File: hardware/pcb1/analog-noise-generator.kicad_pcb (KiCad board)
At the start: 2 copper layers, 12.7 x 53 mm, 77 parts, among them J1 USB_C_Receptacle_USB2.0, J2 Conn_01x03_Pin, J5 Conn_01x04_Pin, J6 Conn_01x04_Pin, J7 Conn_01x02_Pin, J9 Conn_02x04_Odd_Even, U1 STM32F072CBTx, U2 USBLC6-2SC6, U3 LR8321A-T33, U4 LIS2DH12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

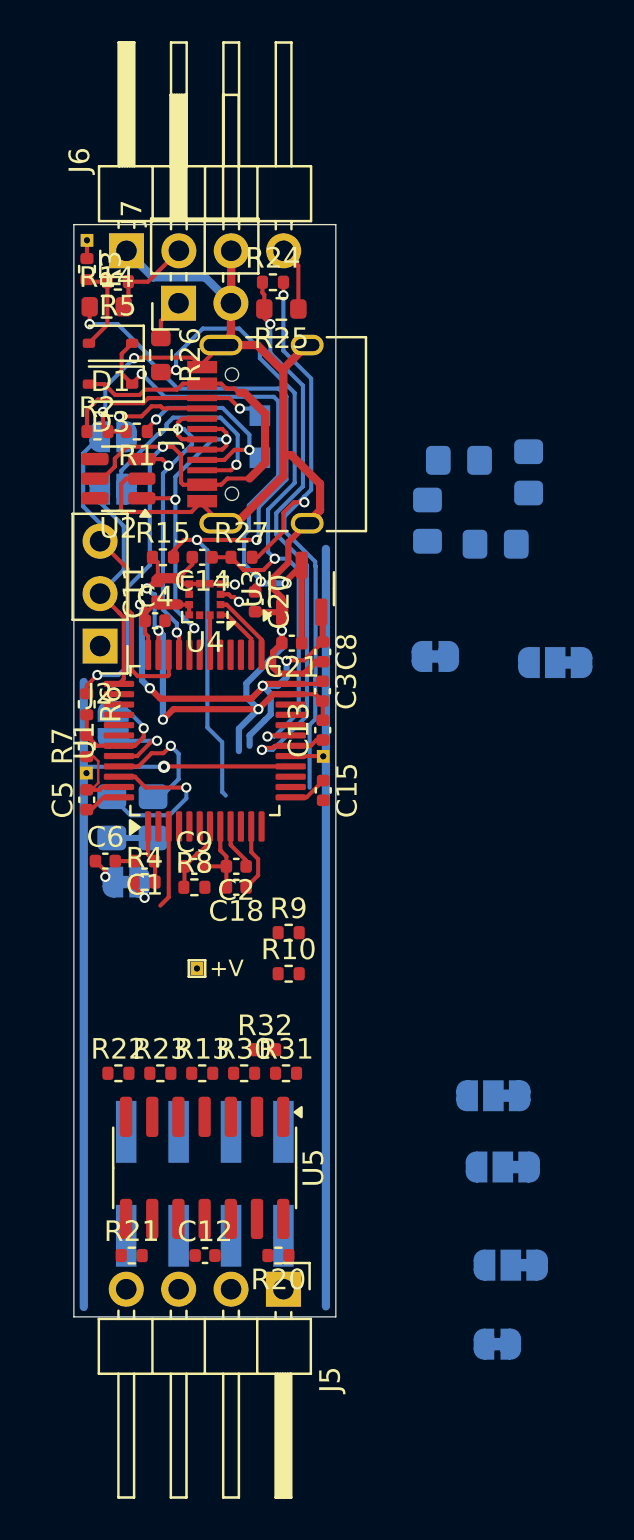
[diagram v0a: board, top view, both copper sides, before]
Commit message: switch to four layers and continue routing
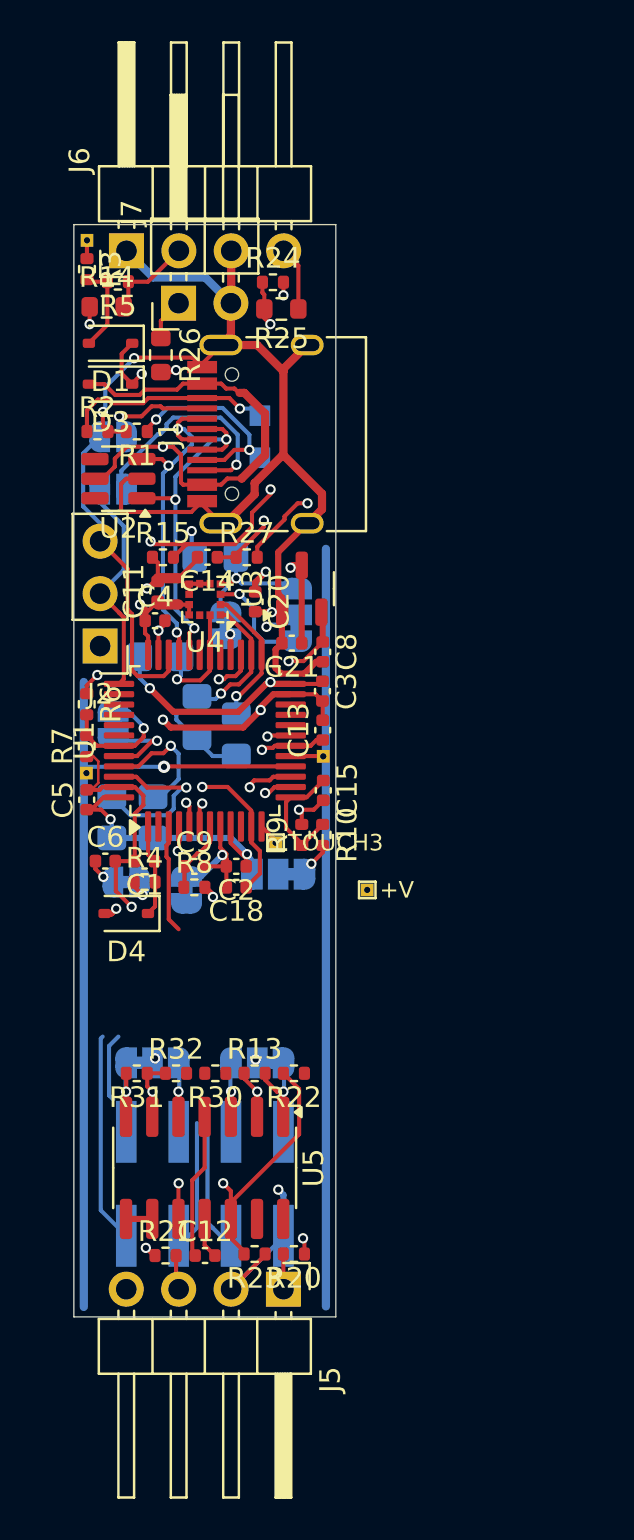
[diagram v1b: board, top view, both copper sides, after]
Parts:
- added D4: ~, Diode_SMD:D_SOD-323, F.Cu at (108.0, 89.9)
- added TP8: TOUCH3, analog-noise-generator:TestPoint_THTPad_small, F.Cu at (115.2, 86.5)
- moved JP12 26.7 mm to (110.9, 88.8), turned to -90 degrees
- moved JP10 22.1 mm to (115.3, 88.0)
- moved R16 19.1 mm to (113.3, 81.3), turned to -90 degrees
- moved JP6 17.7 mm to (109.2, 97.2), turned to 0 degrees
- moved R17 16.7 mm to (111.4, 80.4), turned to -90 degrees
- moved R19 14.5 mm to (109.6, 77.5), turned to 180 degrees
- moved JP8 12.8 mm to (116.2, 75.4), turned to 90 degrees
- moved R18 12.7 mm to (112.3, 72.6)
- moved JP4 11.6 mm to (114.3, 97.2)
- moved JP5 10.3 mm to (112.8, 75.9), turned to 90 degrees
- moved R23 9.88 mm to (114.2, 106.4), turned to 180 degrees
- moved TP4 9.09 mm to (119.6, 88.8)
- moved R22 8.51 mm to (116.1, 97.7), turned to 180 degrees
- moved R31 7.24 mm to (108.5, 97.7), turned to 180 degrees
- moved R10 6.93 mm to (117.5, 86.1), turned to -90 degrees
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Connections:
- net Net-(JP10-C) renamed /AVCC
- net Net-(JP12-B) renamed /AGND
- JP4 pad 2: /OUT1 -> Net-(JP4-C)
- JP6 pad 2: /OUT2 -> Net-(JP6-C)
- R13 pad 2: Net-(R13-Pad2) -> Net-(JP4-A)
- R20 pad 1: Net-(R13-Pad2) -> Net-(JP4-C)
- R20 pad 2: Net-(JP4-A) -> /OUT1
- R21 pad 1: Net-(R21-Pad1) -> Net-(JP6-C)
- R21 pad 2: Net-(JP6-A) -> /OUT2
- R31 pad 2: Net-(R21-Pad1) -> Net-(JP6-A)
- U1 pad 12: unconnected-(U1-PA2-Pad12) -> /TOUCH3
- U5 pad 1: Net-(R13-Pad2) -> Net-(JP4-A)
- U5 pad 7: Net-(R21-Pad1) -> Net-(JP6-A)
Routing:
- net GND: track 96.0 -> 148.4 mm, vias 7 -> 11
- net +3.3V: track 32.3 -> 69.2 mm, vias 4 -> 9
- net /SCK: track 2.74 -> 24.1 mm, vias 0 -> 1
- net +8V: track 26.9 -> 43.9 mm, vias 3 -> 4
- net Net-(U5C-+): track 0.00 -> 16.5 mm, vias 0 -> 2
- net /MOSI: track 0.00 -> 16.4 mm, vias 0 -> 1
- net /EPD_BUSY: track 4.01 -> 15.5 mm
- net Net-(JP4-C): track 0.00 -> 10.4 mm, vias 0 -> 2
- net Net-(JP6-C): track 0.00 -> 10.4 mm, vias 0 -> 2
- net /EPD_DC: track 0.00 -> 10.3 mm, vias 0 -> 1
- net /EPD_RES: track 0.00 -> 10.1 mm, vias 0 -> 1
- net /DAC2: track 0.00 -> 9.72 mm, vias 0 -> 2
- net /DAC1: track 0.00 -> 8.41 mm, vias 0 -> 2
- net /MISO: track 0.00 -> 7.21 mm, vias 0 -> 2
- net /AVCC: track 0.00 -> 7.03 mm
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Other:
- copper layers 2 -> 4

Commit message: finish routing
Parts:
- added TP10: AGND, analog-noise-generator:TestPoint_THTPad_small, B.Cu at (106.7, 96.5)
- added TP11: AVCC, analog-noise-generator:TestPoint_THTPad_small, B.Cu at (106.7, 95.5)
- added TP9: GND, analog-noise-generator:TestPoint_THTPad_small, B.Cu at (116.8, 96.5)
- TP4: moved to B.Cu
- moved JP6 7.42 mm to (110.1, 89.8)
- moved JP4 7.41 mm to (115.1, 89.8)
- moved R13 7.38 mm to (114.6, 90.3)
- moved R22 7.38 mm to (116.5, 90.3)
- moved C12 7.37 mm to (111.8, 99.1)
- moved J9 7.37 mm to (111.8, 95.7)
- moved R20 7.37 mm to (116.1, 99.1)
- moved R21 7.37 mm to (109.9, 99.1)
- moved R23 7.37 mm to (114.2, 99.1)
- moved R30 7.37 mm to (112.3, 90.3)
- moved R31 7.37 mm to (108.5, 90.3)
- moved R32 7.37 mm to (110.4, 90.3)
- moved U5 7.37 mm to (111.8, 94.9)
- moved J5 7.29 mm to (115.6, 100.8)
- moved TP4 7.29 mm to (116.8, 95.5), turned to 180 degrees
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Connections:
- U1 pad 4: /EPD_DC -> /EPD_CS
- U1 pad 5: /EPD_CS -> /EPD_RES
- U1 pad 6: /EPD_RES -> /EPD_DC
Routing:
- net /Vmiddle: track 37.7 -> 55.7 mm, vias 2 -> 3
- net /AGND: track 1.98 -> 19.4 mm, vias 0 -> 2
- net /AVCC: track 7.03 -> 22.7 mm, vias 0 -> 2
- net GND: track 148.4 -> 161.5 mm
- net +3.3V: track 69.2 -> 78.4 mm, vias 9 -> 11
- net /TOUCH1: track 40.4 -> 33.0 mm
- net /TOUCH2: track 38.5 -> 31.1 mm
- net +8V: track 43.9 -> 51.3 mm
- net /EPD_DC: track 10.3 -> 16.5 mm, vias 1 -> 2
- net /MOSI: track 16.4 -> 21.9 mm, vias 1 -> 2
- net /DAC2: track 9.72 -> 14.0 mm, vias 2 -> 3
- net /EPD_CS: track 6.73 -> 10.4 mm, vias 1 -> 2
- net /SCK: track 24.1 -> 27.8 mm, vias 1 -> 2
- net /DAC1: track 8.41 -> 11.6 mm, vias 2 -> 3
- net /EPD_RES: track 10.1 -> 11.5 mm, vias 1 -> 2
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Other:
- board size 12.7 x 53 mm -> 12.7 x 45.6 mm

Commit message: improve silk
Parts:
- added QR1: QR_git_3.8, analog-noise-generator-qr:QR_git_3.8, B.Cu at (107.6, 61.8)
- TP6: value TOUCH1 -> T1
- TP7: value TOUCH2 -> T2
- TP8: value TOUCH3 -> T3; moved to B.Cu
- moved TP8 0.25 mm to (115.2, 85.5), turned to 180 degrees
- turned D1 to 0 degrees
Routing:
- net /IN2L: track 32.4 -> 28.9 mm
- net +8V: track 51.3 -> 49.8 mm
- net GND: track 161.5 -> 160.7 mm, vias 11 -> 10
- net Net-(J1-CC1): track 9.95 -> 9.31 mm
- net /Vmiddle: track 55.7 -> 55.1 mm
- net /VIN_sense: track 47.0 -> 47.5 mm
- net +3.3V: track 78.4 -> 77.9 mm
- net Net-(U5A--): track 3.64 -> 3.48 mm, vias 1 -> 0
- net Net-(U5B--): track 3.20 -> 3.10 mm, vias 1 -> 0
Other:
- board text added: "1"
- board text added: "2"
- board text added: "3V3"
- board text added: "G"
- board text added: "GATE"
- board text added: "GND"
- board text added: "IN1"
- board text added: "IN2"
- board text added: "SWCLK"
- board text added: "SWDIO"
- board text added: "analog noise"
- board text added: "snowball"
- board text added: "v1"

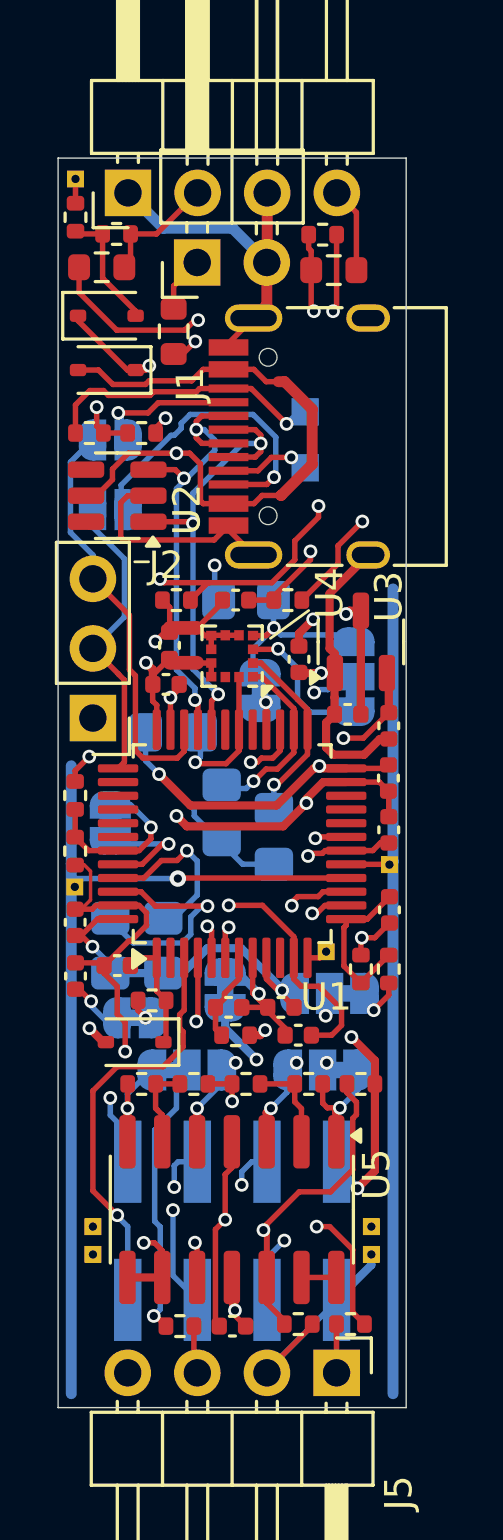
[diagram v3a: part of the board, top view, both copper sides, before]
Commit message: add some LEDs
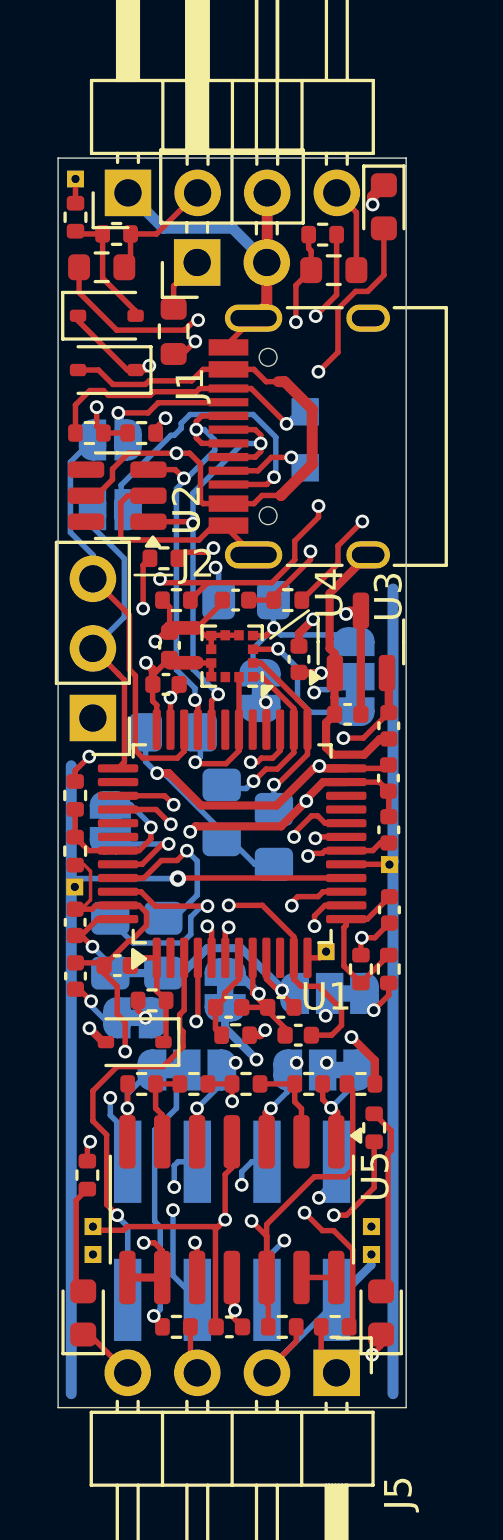
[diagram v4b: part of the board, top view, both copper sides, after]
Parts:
- added D5: white, LED_SMD:LED_0603_1608Metric, F.Cu at (117.2, 98.7)
- added D6: yellow, LED_SMD:LED_0603_1608Metric, F.Cu at (106.3, 98.7)
- added D7: red, LED_SMD:LED_0603_1608Metric, F.Cu at (117.3, 58.3)
- added R33: 1k, Resistor_SMD:R_0402_1005Metric, F.Cu at (116.9, 91.9)
- added R34: 2k2, Resistor_SMD:R_0402_1005Metric, F.Cu at (106.5, 93.6)
- added R35: 2k2, Resistor_SMD:R_0402_1005Metric, F.Cu at (109.3, 71.1)
- TP6: value T1 -> TOUCH1
- TP7: value T2 -> TOUCH2
- TP8: value T3 -> TOUCH3
- moved R23 0.59 mm to (113.6, 99.2)
- moved R20 0.57 mm to (115.5, 99.2)
- moved R21 0.13 mm to (109.7, 99.2)
- moved C12 0.11 mm to (111.7, 99.2)
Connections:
- U1 pad 20: unconnected-(U1-PB2-Pad20) -> /LED1
- U1 pad 39: unconnected-(U1-PB3-Pad39) -> /LED3
- U1 pad 40: unconnected-(U1-PB4-Pad40) -> /LED2
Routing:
- net /LED1: track 0.00 -> 23.2 mm, vias 0 -> 2
- net /LED2: track 0.00 -> 17.9 mm, vias 0 -> 2
- net Net-(D7-A): track 0.00 -> 16.9 mm, vias 0 -> 2
- net /LED3: track 0.00 -> 12.6 mm, vias 0 -> 2
- net GND: track 160.7 -> 172.4 mm, vias 10 -> 12
- net Net-(D5-A): track 0.00 -> 6.89 mm
- net Net-(D6-A): track 0.00 -> 4.01 mm
- net +3.3V: track 77.9 -> 80.8 mm
- net /Vmiddle: track 55.1 -> 56.3 mm
- net /DAC2: track 14.0 -> 13.3 mm

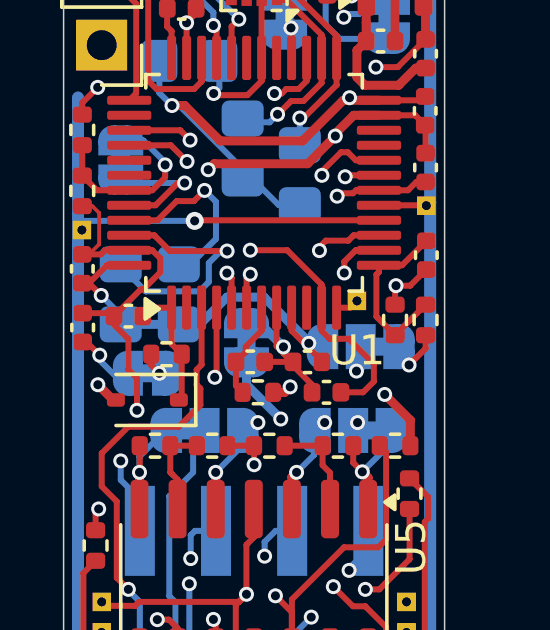
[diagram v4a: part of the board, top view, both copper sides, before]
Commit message: add testpoint for 3.3V
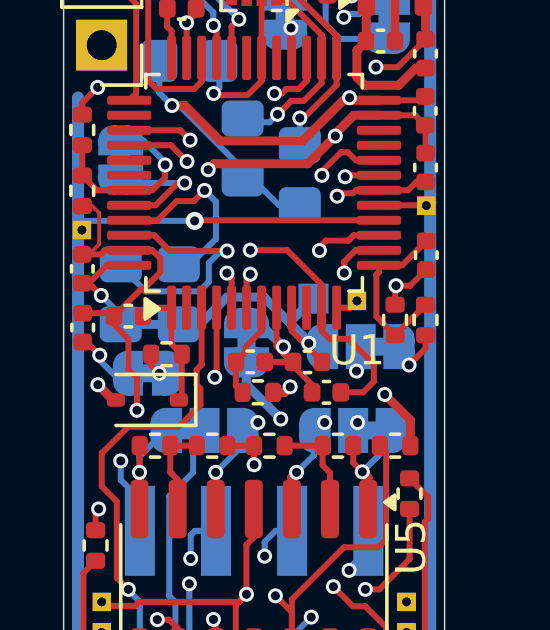
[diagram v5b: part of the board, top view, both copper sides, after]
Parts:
- added TP12: 3V3, TestPoint:TestPoint_Pad_1.0x1.0mm, B.Cu at (113.7, 85.4)
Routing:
- net +3.3V: track 80.8 -> 81.9 mm
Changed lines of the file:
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@@
     (property "ki_keywords" "R res resistor")
     (attr smd exclude_from_bom)
-    (fp_text reference "R16" (at 0.381 -1.397 90) (layer "B.SilkS")
+    (fp_text reference "R16" (at 0.3048 -1.27 90) (layer "B.SilkS")
         (effects (font (size 0.8 0.8) (thickness 0.12)) (justify mirror))
     )
@@
       ))
   )
+  (footprint "TestPoint:TestPoint_Pad_1.0x1.0mm" (layer "B.Cu")
+    (at 113.7412 85.3948)
+    (descr "SMD rectangular pad as test Point, square 1.0mm side length")
+    (tags "test point SMD pad rectangle square")
+    (property "Sheetfile" "analog-noise-generator.kicad_sch")
+    (property "Sheetname" "")
+    (property "exclude_from_bom" "")
+    (property "ki_description" "test point (alternative probe-style design)")
+    (property "ki_keywords" "test point tp")
+    (attr exclude_from_pos_files exclude_from_bom)
+    (fp_text reference "TP12" (at 0 1.448 180) (layer "B.SilkS") hide
+        (effects (font (size 1 1) (thickness 0.15)) (justify mirror))
+    )
+    (fp_text value "3V3" (at -0.2032 -1.3716 180) (layer "B.SilkS")
+        (effects (font (size 0.8 0.8) (thickness 0.12)) (justify mirror))
+    )
+    (fp_text user "${REFERENCE}" (at 0 1.45 180) (layer "B.Fab")
+        (effects (font (size 1 1) (thickness 0.15)) (justify mirror))
+    )
+    (fp_line (start -0.7 -0.7) (end -0.7 0.7)
+      (stroke (width 0.12) (type solid)) (layer "B.SilkS"))
+    (fp_line (start -0.7 0.7) (end 0.7 0.7)
+      (stroke (width 0.12) (type solid)) (layer "B.SilkS"))
+    (fp_line (start 0.7 -0.7) (end -0.7 -0.7)
+      (stroke (width 0.12) (type solid)) (layer "B.SilkS"))
+    (fp_line (start 0.7 0.7) (end 0.7 -0.7)
+      (stroke (width 0.12) (type solid)) (layer "B.SilkS"))
+    (fp_line (start -1 1) (end -1 -1)
+      (stroke (width 0.05) (type solid)) (layer "B.CrtYd"))
+    (fp_line (start -1 1) (end 1 1)
+      (stroke (width 0.05) (type solid)) (layer "B.CrtYd"))
+    (fp_line (start 1 -1) (end -1 -1)
+      (stroke (width 0.05) (type solid)) (layer "B.CrtYd"))
+    (fp_line (start 1 -1) (end 1 1)
+      (stroke (width 0.05) (type solid)) (layer "B.CrtYd"))
+    (pad "1" smd rect (at 0 0) (size 1 1) (layers "B.Cu" "B.Mask")
+      (net 3 "+3.3V") (pinfunction "1") (pintype "passive"))
+  )
   (footprint "Resistor_SMD:R_0805_2012Metric_Pad1.20x1.40mm_HandSolder" (layer "B.Cu")
     (at 109.601 77.47 180)
@@
     (attr exclude_from_pos_files)
     (net_tie_pad_groups "1, 2")
-    (fp_text reference "JP12" (at -1.905 -1.651 -180) (layer "B.SilkS")
+    (fp_text reference "JP12" (at -3.048 -0.1016 -90) (layer "B.SilkS")
         (effects (font (size 0.8 0.8) (thickness 0.12)) (justify mirror))
     )
@@
     (property "ki_keywords" "R res resistor")
     (attr smd exclude_from_bom)
-    (fp_text reference "R28" (at -1.053 -1.367 90) (layer "B.SilkS")
+    (fp_text reference "R28" (at -0.8498 -1.367 90) (layer "B.SilkS")
         (effects (font (size 0.8 0.8) (thickness 0.12)) (justify mirror))
     )
@@
         (effects (font (size 1 1) (thickness 0.15)) (justify mirror))
     )
-    (fp_text value "TOUCH3" (at -0.889 1.016) (layer "B.SilkS")
+    (fp_text value "TOUCH3" (at -0.3302 5.2578 270) (layer "B.SilkS")
         (effects (font (size 0.8 0.8) (thickness 0.12)) (justify left mirror))
     )
@@
         (effects (font (size 1 1) (thickness 0.15)) (justify mirror))
     )
-    (fp_text value "TOUCH1" (at 0.4 -0.1778) (layer "B.SilkS")
+    (fp_text value "TOUCH1" (at 0.4 -0.2032) (layer "B.SilkS")
         (effects (font (size 0.8 0.8) (thickness 0.12)) (justify right mirror))
     )
@@
   (segment (start 113.284 82.28) (end 112.584 82.28) (width 0.2) (layer "B.Cu") (net 3))
   (segment (start 112.584 82.28) (end 109.263 78.959) (width 0.2) (layer "B.Cu") (net 3))
-  (segment (start 113.582839 86.837305) (end 112.089534 85.344) (width 0.3) (layer "B.Cu") (net 3))
   (segment (start 110.86 85.344) (end 109.95 86.254) (width 0.3) (layer "B.Cu") (net 3))
+  (segment (start 112.915367 86.169833) (end 112.089534 85.344) (width 0.3) (layer "B.Cu") (net 3))
   (segment (start 109.263 78.959) (end 109.0224 78.959) (width 0.2) (layer "B.Cu") (net 3))
   (segment (start 107.25 85.875032) (end 107.25 86.254) (width 0.2) (layer "B.Cu") (net 3))
   (segment (start 115.57 93.809625) (end 114.925697 94.453928) (width 0.3) (layer "B.Cu") (net 3))
+  (segment (start 113.582839 86.837305) (end 112.915367 86.169833) (width 0.3) (layer "B.Cu") (net 3))
   (segment (start 108.601 77.597) (end 108.601 78.5376) (width 0.2) (layer "B.Cu") (net 3))
   (segment (start 113.941203 87.242363) (end 114.016 87.242363) (width 0.2) (layer "B.Cu") (net 3))
+  (segment (start 112.915367 86.169833) (end 112.966167 86.169833) (width 0.3) (layer "B.Cu") (net 3))
+  (segment (start 112.966167 86.169833) (end 113.7412 85.3948) (width 0.3) (layer "B.Cu") (net 3))
   (segment (start 111.268 72.644) (end 111.268 71.567404) (width 0.2) (layer "B.Cu") (net 3))
   (segment (start 108.601 78.5376) (end 109.0224 78.959) (width 0.2) (layer "B.Cu") (net 3))
@@
   (segment (start 116.574815 69.711815) (end 116.511315 69.775315) (width 0.2) (layer "In1.Cu") (net 19))
   (segment (start 117.475 80.137) (end 116.322 81.29) (width 0.2) (layer "In1.Cu") (net 19))
-  (segment (start 116.574815 63.638186) (end 115.217437 62.280808) (width 0.2) (layer "In1.Cu") (net 19))
-  (segment (start 116.574815 69.711815) (end 116.574815 63.638186) (width 0.2) (layer "In1.Cu") (net 19))
+  (segment (start 114.808 62.5348) (end 114.808 62.280808) (width 0.2) (layer "In1.Cu") (net 19))
   (segment (start 115.623 71.326371) (end 116.091629 71.795) (width 0.2) (layer "In1.Cu") (net 19))
   (segment (start 116.706556 71.795) (end 117.475 72.563444) (width 0.2) (layer "In1.Cu") (net 19))
   (segment (start 116.1232 95.313286) (end 114.262486 97.174) (width 0.2) (layer "In1.Cu") (net 19))
   (segment (start 117.475 72.563444) (end 117.475 80.137) (width 0.2) (layer "In1.Cu") (net 19))
+  (segment (start 116.574815 69.711815) (end 116.574815 64.301615) (width 0.2) (layer "In1.Cu") (net 19))
   (segment (start 116.322 81.29) (end 116.322 83.63782) (width 0.2) (layer "In1.Cu") (net 19))
   (segment (start 116.967 90.1446) (end 116.1232 90.9884) (width 0.2) (layer "In1.Cu") (net 19))
@@
   (segment (start 116.091629 71.795) (end 116.706556 71.795) (width 0.2) (layer "In1.Cu") (net 19))
   (segment (start 117.094 84.40982) (end 117.094 85.471) (width 0.2) (layer "In1.Cu") (net 19))
-  (segment (start 115.217437 62.280808) (end 114.808 62.280808) (width 0.2) (layer "In1.Cu") (net 19))
   (segment (start 114.262486 97.174) (end 109.6123 97.174) (width 0.2) (layer "In1.Cu") (net 19))
   (segment (start 116.574815 69.711815) (end 115.623 70.66363) (width 0.2) (layer "In1.Cu") (net 19))
@@
   (segment (start 116.332 86.233) (end 116.332 87.867662) (width 0.2) (layer "In1.Cu") (net 19))
   (segment (start 116.322 83.63782) (end 117.094 84.40982) (width 0.2) (layer "In1.Cu") (net 19))
+  (segment (start 116.574815 64.301615) (end 114.808 62.5348) (width 0.2) (layer "In1.Cu") (net 19))
   (segment (start 111.628 67.925) (end 112.703815 67.925) (width 0.2) (layer "F.Cu") (net 20))
   (segment (start 108.968 66.367248) (end 109.328486 66.006762) (width 0.2) (layer "F.Cu") (net 20))
